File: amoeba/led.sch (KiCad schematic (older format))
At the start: 3 parts

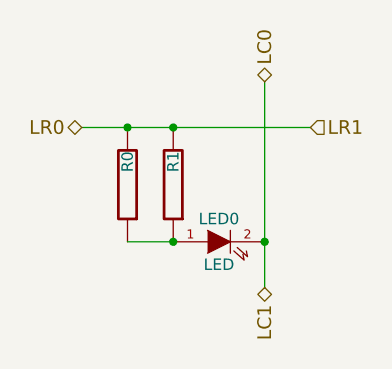
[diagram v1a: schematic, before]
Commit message: Adding net names to amoeba.
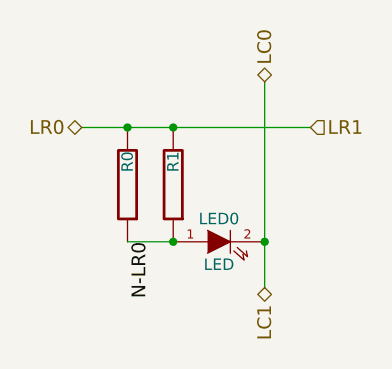
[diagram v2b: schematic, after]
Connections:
- net N-LR0: now reaches LED0.1 (A), R0.1, R1.1
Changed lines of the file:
@@
 Sheet 3 4
 Title ""
-Date "13 sep 2015"
+Date "15 sep 2015"
 Rev ""
 Comp ""
@@
 Connection ~ 5300 3350
 Connection ~ 5500 3350
+Text Label 5400 3850 3    60   ~ 0
+N-LR0
 $EndSCHEMATC
